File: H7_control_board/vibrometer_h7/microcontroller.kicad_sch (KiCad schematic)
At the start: 36 parts, among them J3 Conn_01x04_Socket, J4 Conn_ST_STDC14, Q201 BSS138, Q202 BSS138, SW201 SW_Push, U1 STM32H723VGTx, Y201 24MHz

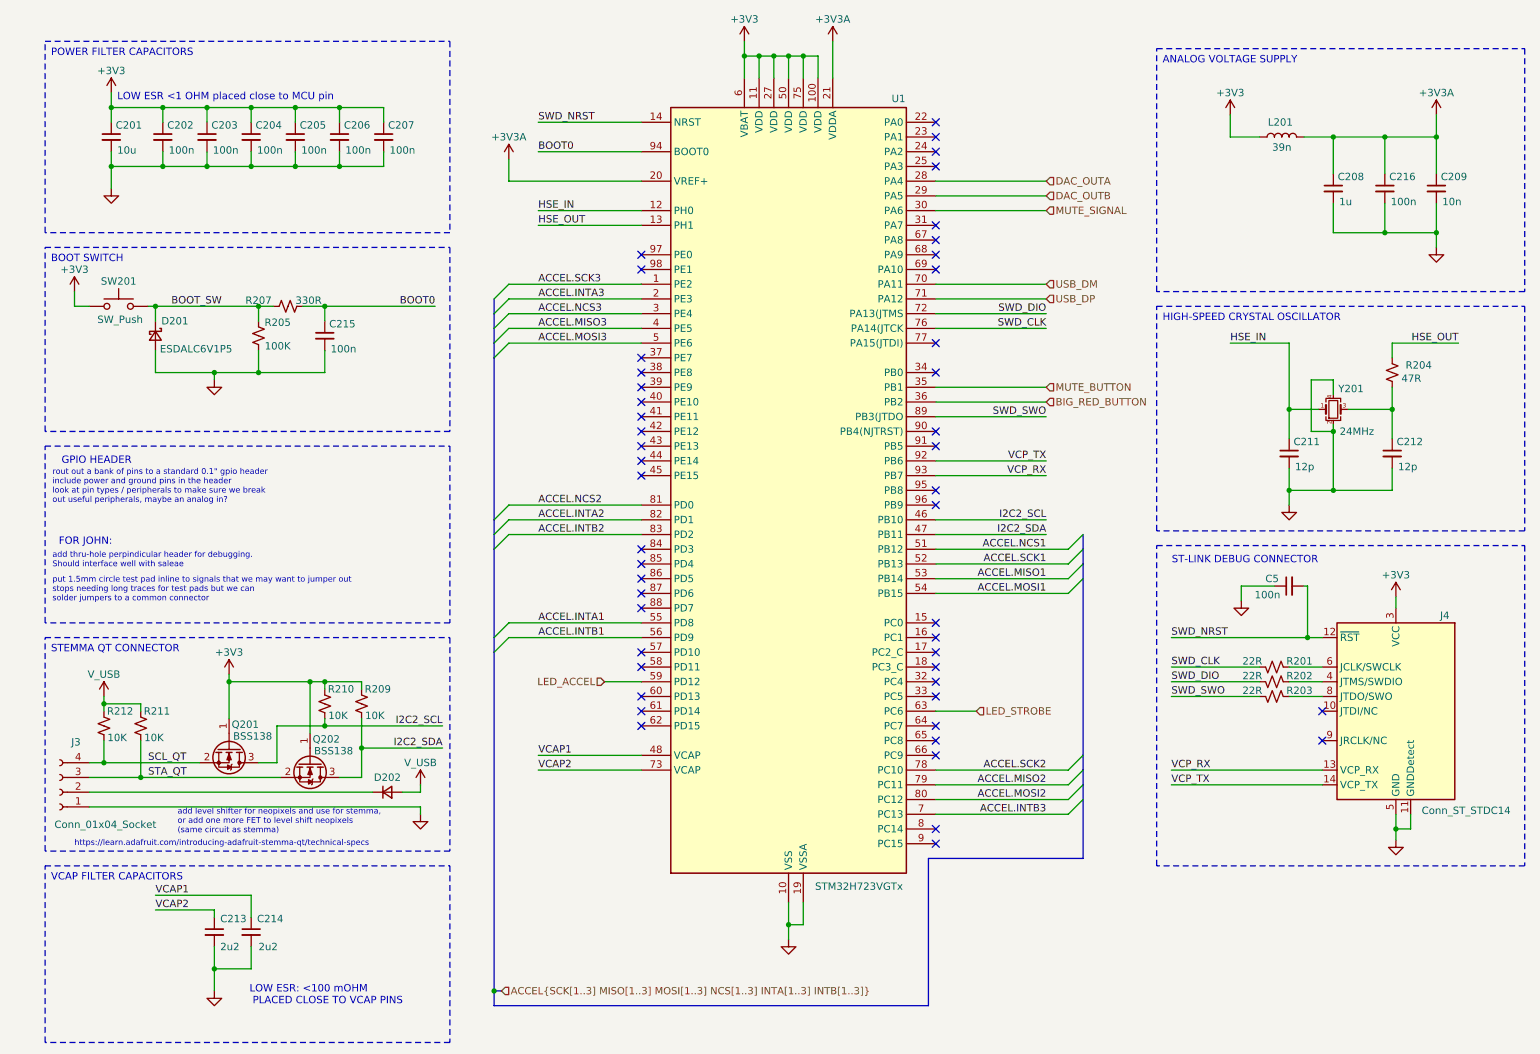
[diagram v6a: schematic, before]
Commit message: updated reference designator naming
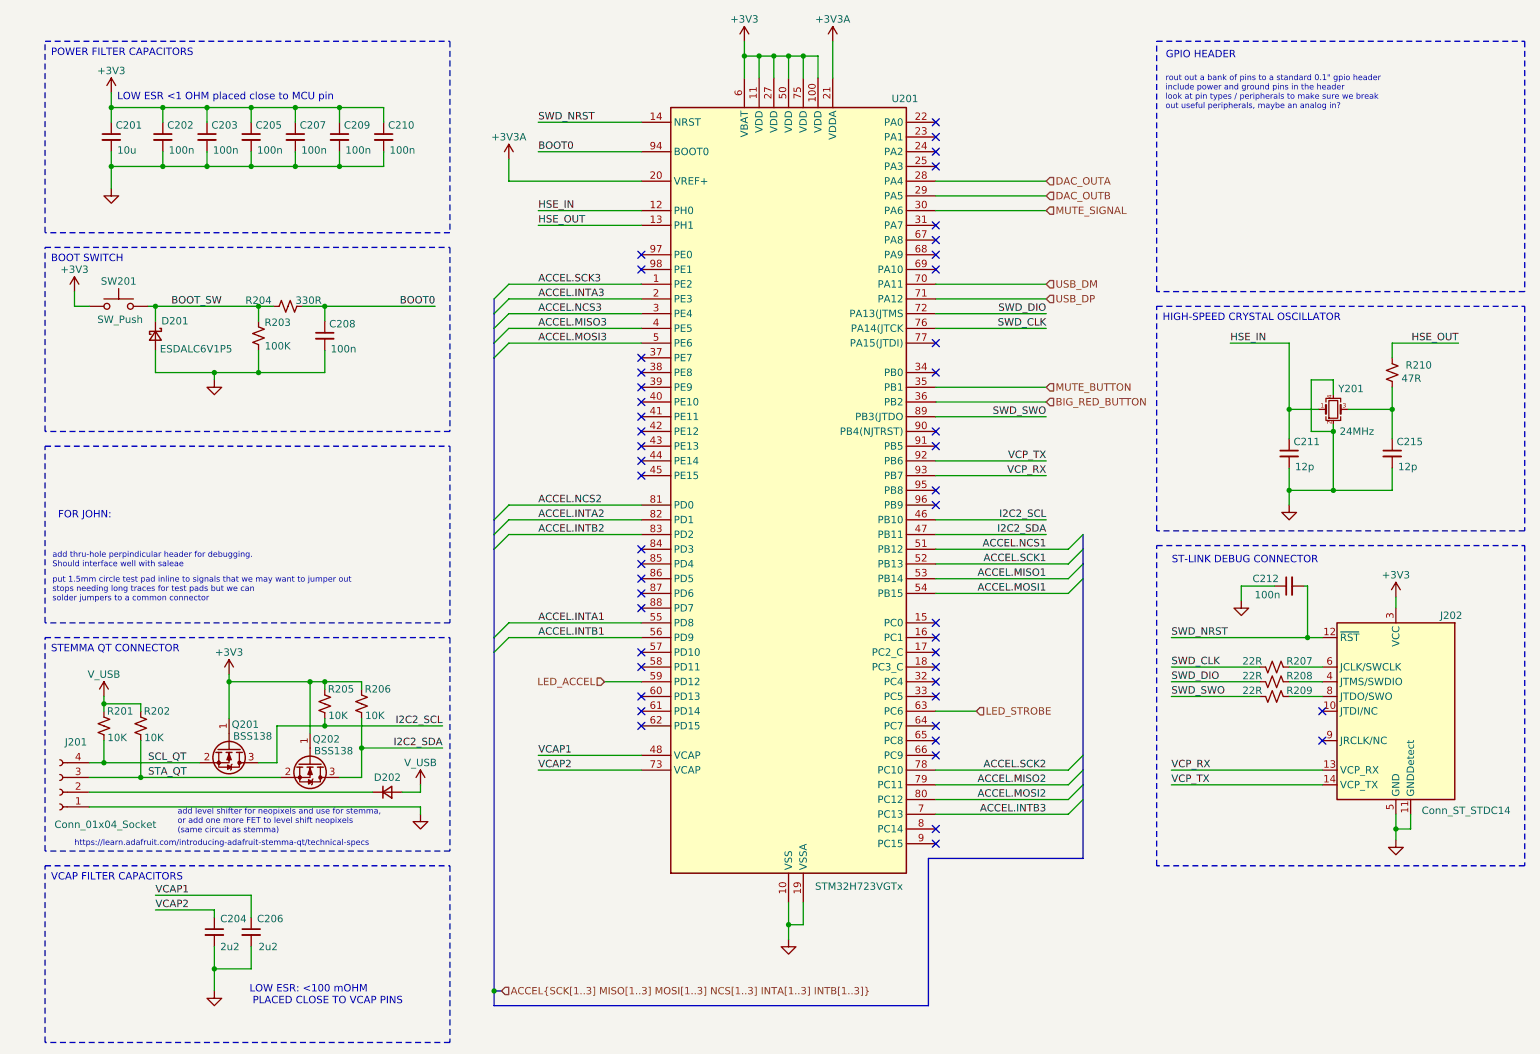
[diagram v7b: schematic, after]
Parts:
- removed C208: 1u, Capacitor_SMD:C_0805_2012Metric, symbol Device:C_Small
- removed C209: 10n, Capacitor_SMD:C_0603_1608Metric, symbol Device:C_Small
- removed C216: 100n, Capacitor_SMD:C_0402_1005Metric_Pad0.74x0.62mm_HandSolder, symbol Device:C_Small
- removed L201: 39n, symbol Device:L
- renumbered C213 to C204, C204 to C205, C214 to C206, C205 to C207, C215 to C208, C206 to C209, C207 to C210, C5 to C212, C212 to C215, J3 to J201, J4 to J202, R212 to R201, R211 to R202, R205 to R203, R207 to R204, R210 to R205, R209 to R206, R201 to R207, R202 to R208, R203 to R209, R204 to R210, U1 to U201

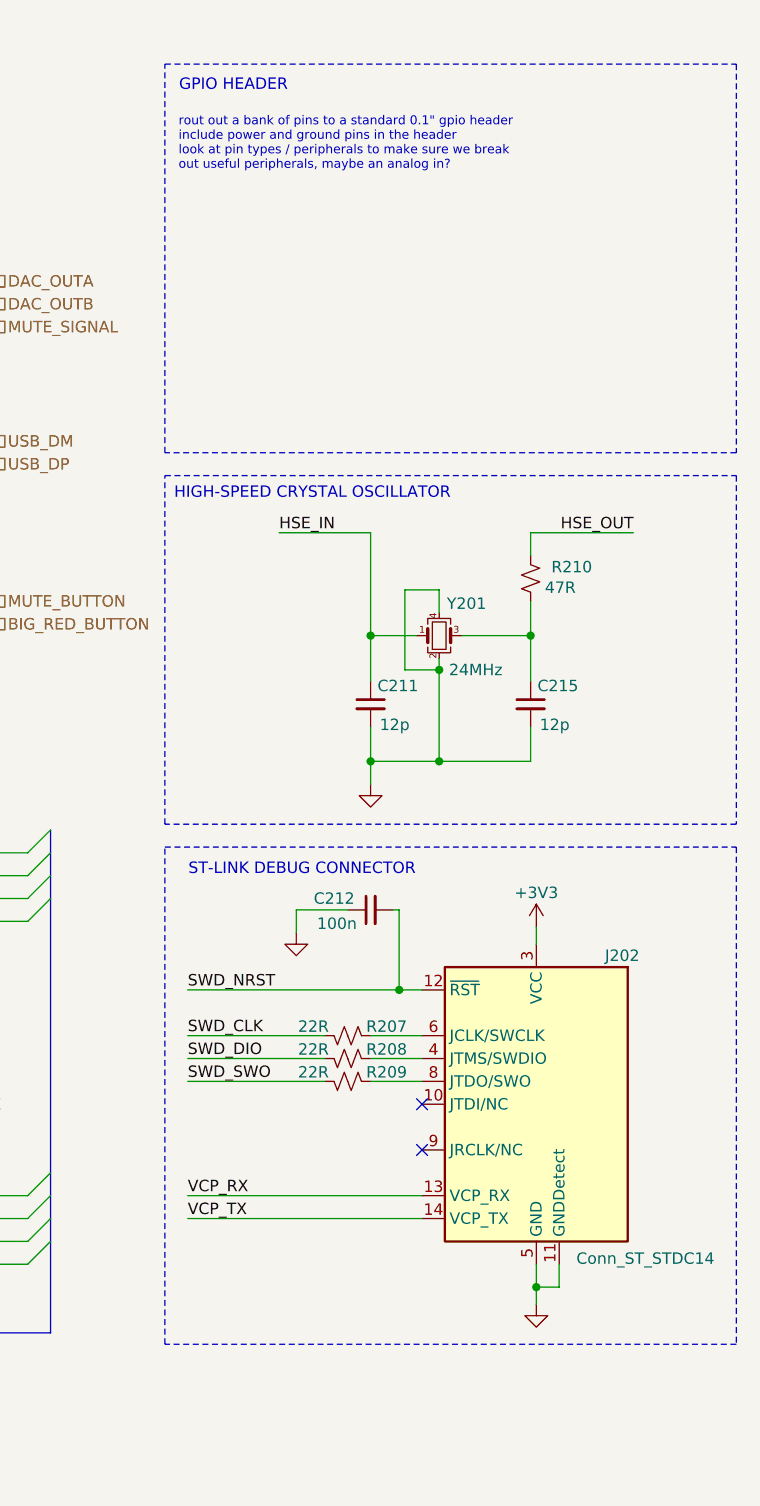
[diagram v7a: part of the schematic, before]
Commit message: updated debug connector
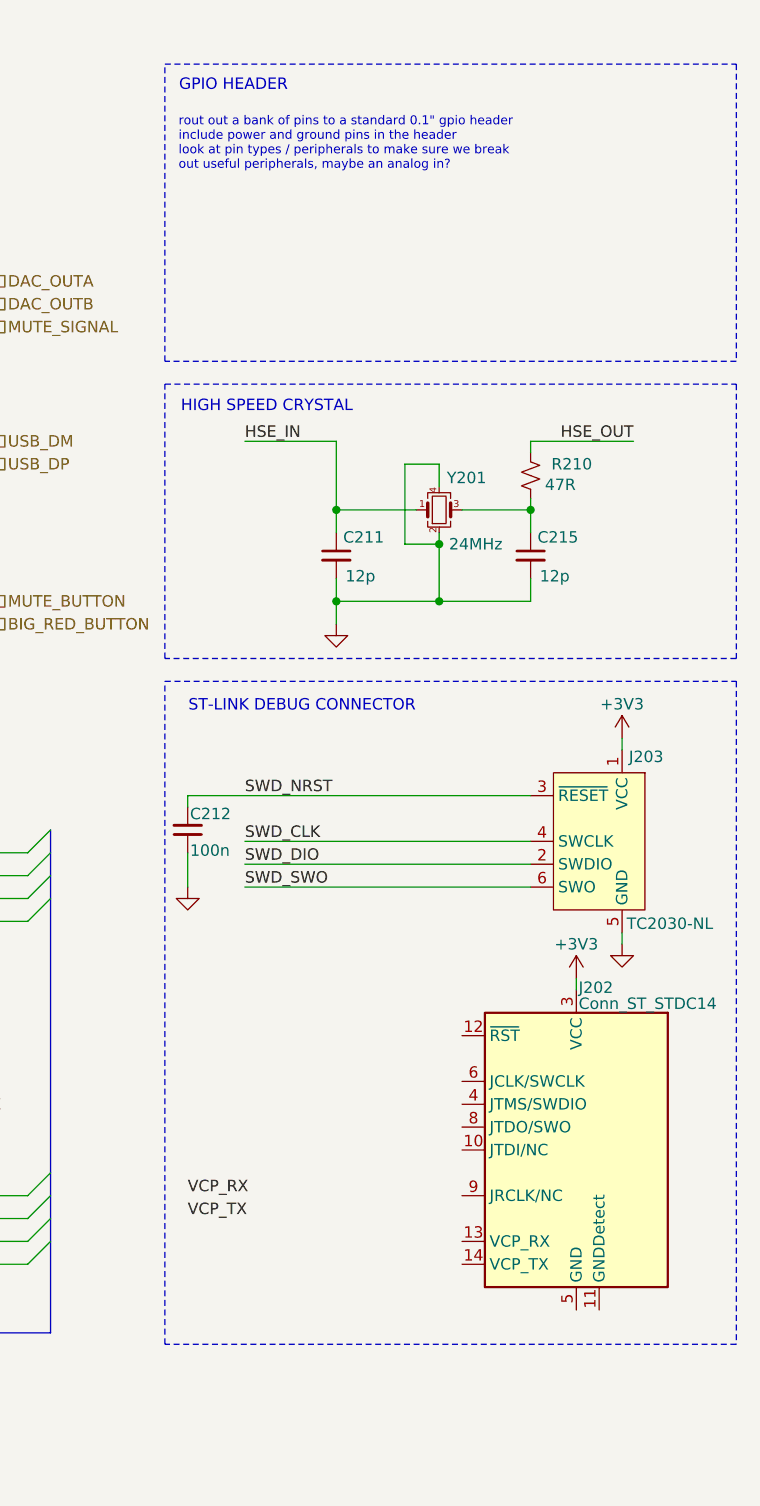
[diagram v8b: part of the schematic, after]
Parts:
- removed R207, R208, R209: 22R, symbol Device:R_Small_US
- added J203: TC2030-NL, Connector:Tag-Connect_TC2030-IDC-NL_2x03_P1.27mm_Vertical, symbol Connector:Conn_ARM_SWD_TagConnect_TC2030-NL
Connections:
- net +3V3: now also J203.1 (VCC)
- net GND: now also J203.5 (GND); no longer J202.11 (GNDDetect), J202.5 (GND), J202.7 (GND)
- net SWD_CLK: now also J203.4 (SWCLK)
- net SWD_DIO: now also J203.2 (SWDIO)
- net SWD_NRST: now also J203.3 (~{RESET}); no longer J202.12 (~{RST})
- net SWD_SWO: now also J203.6 (SWO)
- net VCP_RX: no longer J202.13 (VCP_RX)
- net VCP_TX: no longer J202.14 (VCP_TX)
- new net: J202.5 (GND), J202.7 (GND)
- no-connect marks 48 -> 46
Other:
- note added: "HIGH SPEED CRYSTAL"
- moved on the sheet: C211, C212, C215, J202, R210, Y201
